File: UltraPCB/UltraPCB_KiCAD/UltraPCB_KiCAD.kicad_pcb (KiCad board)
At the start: 2 copper layers, 69 x 112.2 mm, 52 parts, among them J1 USB_C_Receptacle_PowerOnly_6P, J2 Conn_01x04_Pin, Q1 SQ2325ES-T1_GE3, Q2 SQ2325ES-T1_GE3, Q3 SQ2325ES-T1_GE3, Q4 SQ2325ES-T1_GE3, Q5 SQ2325ES-T1_GE3, Q6 IRLML6244, SW1 SW_Push, SW2 SW_Push, U2 LM3670MF-3.3, U3 LTC-4627JD, U4 STM32F030K6Tx

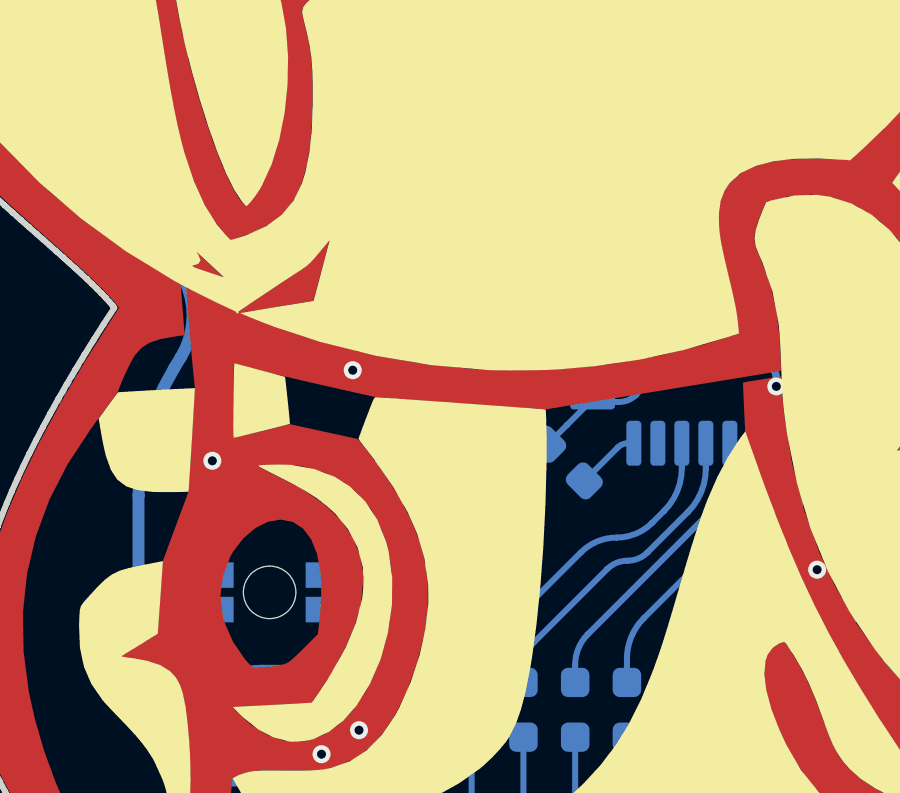
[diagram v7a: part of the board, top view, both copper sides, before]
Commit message: Added quartz
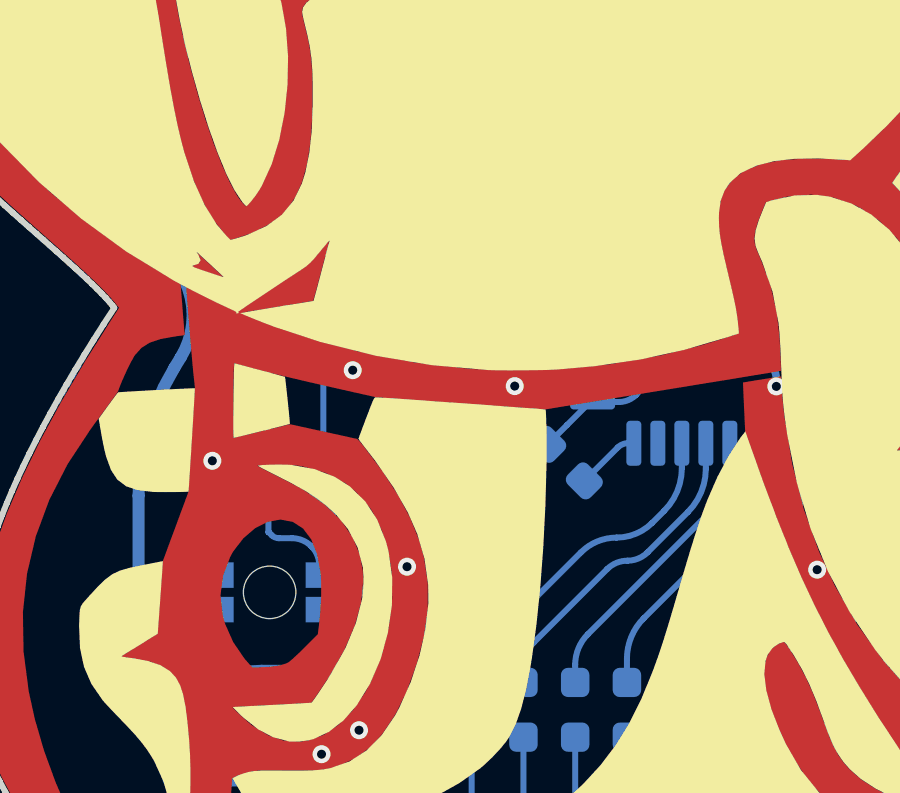
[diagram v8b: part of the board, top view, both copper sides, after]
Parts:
- added Y1: Crystal_GND24, Crystal:Crystal_SMD_3225-4Pin_3.2x2.5mm, B.Cu at (137.7, 117.2)
- moved R11 4.04 mm to (132.0, 119.3)
- moved R12 4.01 mm to (133.9, 119.3)
- moved C7 0.58 mm to (138.7, 113.5)
- moved C6 0.58 mm to (138.7, 111.9)
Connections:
- U4 pad 2: /LED_Blue -> Net-(U4-PF0)
- U4 pad 3: /LED_Red -> Net-(U4-PF1)
- U4 pad 7: unconnected-(U4-PA1-Pad7) -> /LED_Blue
- U4 pad 8: unconnected-(U4-PA2-Pad8) -> /LED_Red
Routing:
- net /LED_Blue: track 6.80 -> 15.4 mm
- net /LED_Red: track 9.02 -> 17.2 mm
- net Net-(U4-PF1): track 0.00 -> 7.40 mm
- net Net-(U4-PF0): track 0.00 -> 4.75 mm
- net +3V3: track 170.7 -> 171.2 mm
- net GND: vias 24 -> 26
